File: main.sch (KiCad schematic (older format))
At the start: 25 parts, among them U3 PT6311, U4 VFD_HNV-12SS62

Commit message: shuffled things around
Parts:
- removed R40, R41, R42, R43, R44, R45, R46, R47: 10K, Resistor_SMD:R_0805_2012Metric, symbol Device:R
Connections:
- net labels removed: K1, K2, K3, K4
- wire segments 147 -> 120
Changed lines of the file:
@@
 	2400 3400 2400 3600
-Wire Wire Line
-	5700 5800 5800 5800
-$Comp
-L Device:R R41
-U 1 1 5F375184
-P 5800 6150
-F 0 "R41" H 5870 6196 50  0000 L CNN
-F 1 "10K" H 5870 6105 50  0000 L CNN
-F 2 "Resistor_SMD:R_0805_2012Metric" V 5730 6150 50  0001 C CNN
-F 3 "~" H 5800 6150 50  0001 C CNN
-	1    5800 6150
-	1    0    0    -1
-$EndComp
-$Comp
-L Device:R R43
-U 1 1 5F3751DC
-P 6100 6000
-F 0 "R43" H 6170 6046 50  0000 L CNN
-F 1 "10K" H 6170 5955 50  0000 L CNN
-F 2 "Resistor_SMD:R_0805_2012Metric" V 6030 6000 50  0001 C CNN
-F 3 "~" H 6100 6000 50  0001 C CNN
-	1    6100 6000
-	1    0    0    -1
-$EndComp
-$Comp
-L Device:R R45
-U 1 1 5F378B77
-P 6400 5850
-F 0 "R45" H 6470 5896 50  0000 L CNN
-F 1 "10K" H 6470 5805 50  0000 L CNN
-F 2 "Resistor_SMD:R_0805_2012Metric" V 6330 5850 50  0001 C CNN
-F 3 "~" H 6400 5850 50  0001 C CNN
-	1    6400 5850
-	1    0    0    -1
-$EndComp
-$Comp
-L Device:R R47
-U 1 1 5F37C669
-P 6700 5700
-F 0 "R47" H 6770 5746 50  0000 L CNN
-F 1 "10K" H 6770 5655 50  0000 L CNN
-F 2 "Resistor_SMD:R_0805_2012Metric" V 6630 5700 50  0001 C CNN
-F 3 "~" H 6700 5700 50  0001 C CNN
-	1    6700 5700
-	1    0    0    -1
-$EndComp
-Wire Wire Line
-	6700 5850 6700 6350
-Wire Wire Line
-	6700 6350 6400 6350
-Wire Wire Line
-	5800 6350 5800 6300
-Wire Wire Line
-	6100 6150 6100 6350
-Connection ~ 6100 6350
-Wire Wire Line
-	6100 6350 5800 6350
-Wire Wire Line
-	6400 6000 6400 6350
-Connection ~ 6400 6350
-Wire Wire Line
-	6400 6350 6250 6350
-Wire Wire Line
-	6250 6350 6250 6400
-Connection ~ 6250 6350
-Wire Wire Line
-	6250 6350 6100 6350
-$Comp
-L power:GND #PWR050
-U 1 1 5F38C73B
-P 6250 6400
-F 0 "#PWR050" H 6250 6150 50  0001 C CNN
-F 1 "GND" H 6255 6227 50  0000 C CNN
-F 2 "" H 6250 6400 50  0001 C CNN
-F 3 "" H 6250 6400 50  0001 C CNN
-	1    6250 6400
-	1    0    0    -1
-$EndComp
-Wire Wire Line
-	6700 5550 6700 5500
-Wire Wire Line
-	6400 5600 6400 5700
-Wire Wire Line
-	6100 5700 6100 5850
-Wire Wire Line
-	5800 5800 5800 6000
-Wire Wire Line
-	6700 5500 6750 5500
-Wire Wire Line
-	6400 5600 6450 5600
-Wire Wire Line
-	6100 5700 6150 5700
-Wire Wire Line
-	5800 5800 5850 5800
-Connection ~ 5800 5800
-Text HLabel 6750 5500 2    50   Input ~ 0
-K1
-Text HLabel 6450 5600 2    50   Input ~ 0
-K2
-Text HLabel 6150 5700 2    50   Input ~ 0
-K3
-Text HLabel 5850 5800 2    50   Input ~ 0
-K4
 Wire Wire Line
 	5350 2550 6500 2550
@@
 	4000 4500 3700 4500
 Wire Wire Line
-	3700 4700 3750 4700
-Wire Wire Line
 	3750 5100 4000 5100
 Wire Wire Line
-	3750 4700 3750 5100
-Wire Wire Line
 	3750 5100 3750 5200
-Connection ~ 3750 5100
 $Comp
 L power:GND #PWR047
@@
 	1800 2800 2250 2800
 $Comp
-L Device:R R44
-U 1 1 5F318CEB
-P 6150 5600
-F 0 "R44" V 5943 5600 50  0000 C CNN
-F 1 "10K" V 6034 5600 50  0000 C CNN
-F 2 "Resistor_SMD:R_0805_2012Metric" V 6080 5600 50  0001 C CNN
-F 3 "~" H 6150 5600 50  0001 C CNN
-	1    6150 5600
-	0    1    1    0
-$EndComp
-Wire Wire Line
-	6100 5700 6000 5700
-Connection ~ 6100 5700
-Wire Wire Line
-	6400 5600 6300 5600
-Connection ~ 6400 5600
-Wire Wire Line
-	6700 5500 6600 5500
-Connection ~ 6700 5500
-$Comp
-L Device:R R46
-U 1 1 5F33290D
-P 6450 5500
-F 0 "R46" V 6243 5500 50  0000 C CNN
-F 1 "10K" V 6334 5500 50  0000 C CNN
-F 2 "Resistor_SMD:R_0805_2012Metric" V 6380 5500 50  0001 C CNN
-F 3 "~" H 6450 5500 50  0001 C CNN
-	1    6450 5500
-	0    1    1    0
-$EndComp
-$Comp
-L Device:R R42
-U 1 1 5F343E3D
-P 5850 5700
-F 0 "R42" V 5643 5700 50  0000 C CNN
-F 1 "10K" V 5734 5700 50  0000 C CNN
-F 2 "Resistor_SMD:R_0805_2012Metric" V 5780 5700 50  0001 C CNN
-F 3 "~" H 5850 5700 50  0001 C CNN
-	1    5850 5700
-	0    1    1    0
-$EndComp
-$Comp
-L Device:R R40
-U 1 1 5F34C8CC
-P 5550 5800
-F 0 "R40" V 5343 5800 50  0000 C CNN
-F 1 "10K" V 5434 5800 50  0000 C CNN
-F 2 "Resistor_SMD:R_0805_2012Metric" V 5480 5800 50  0001 C CNN
-F 3 "~" H 5550 5800 50  0001 C CNN
-	1    5550 5800
-	0    1    1    0
-$EndComp
-Wire Wire Line
-	5350 5500 6300 5500
-Wire Wire Line
-	6000 5600 5350 5600
-Wire Wire Line
-	5350 5700 5700 5700
-Wire Wire Line
-	5400 5800 5350 5800
-$Comp
 L Connector:TestPoint TP1

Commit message: NTC circuit and values added
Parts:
- U3: symbol ThommasSTUFF:PT6311-Custom_modules -> buttonbox2-rescue:PT6311-Custom_modules-ThommasSTUFF
- U4: symbol ThommasSTUFF:VFD_HNV-12SS62-custom_comps -> buttonbox2-rescue:VFD_HNV-12SS62-custom_comps-ThommasSTUFF
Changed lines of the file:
@@
 $EndDescr
 $Comp
-L ThommasSTUFF:PT6311-Custom_modules U?
+L buttonbox2-rescue:PT6311-Custom_modules-ThommasSTUFF U?
 U 1 1 5F3F0EEF
 P 4650 2250
@@
 	5350 2350 5400 2350
 $Comp
-L ThommasSTUFF:VFD_HNV-12SS62-custom_comps U?
+L buttonbox2-rescue:VFD_HNV-12SS62-custom_comps-ThommasSTUFF U?
 U 1 1 5F3F0F03
 P 7500 1700

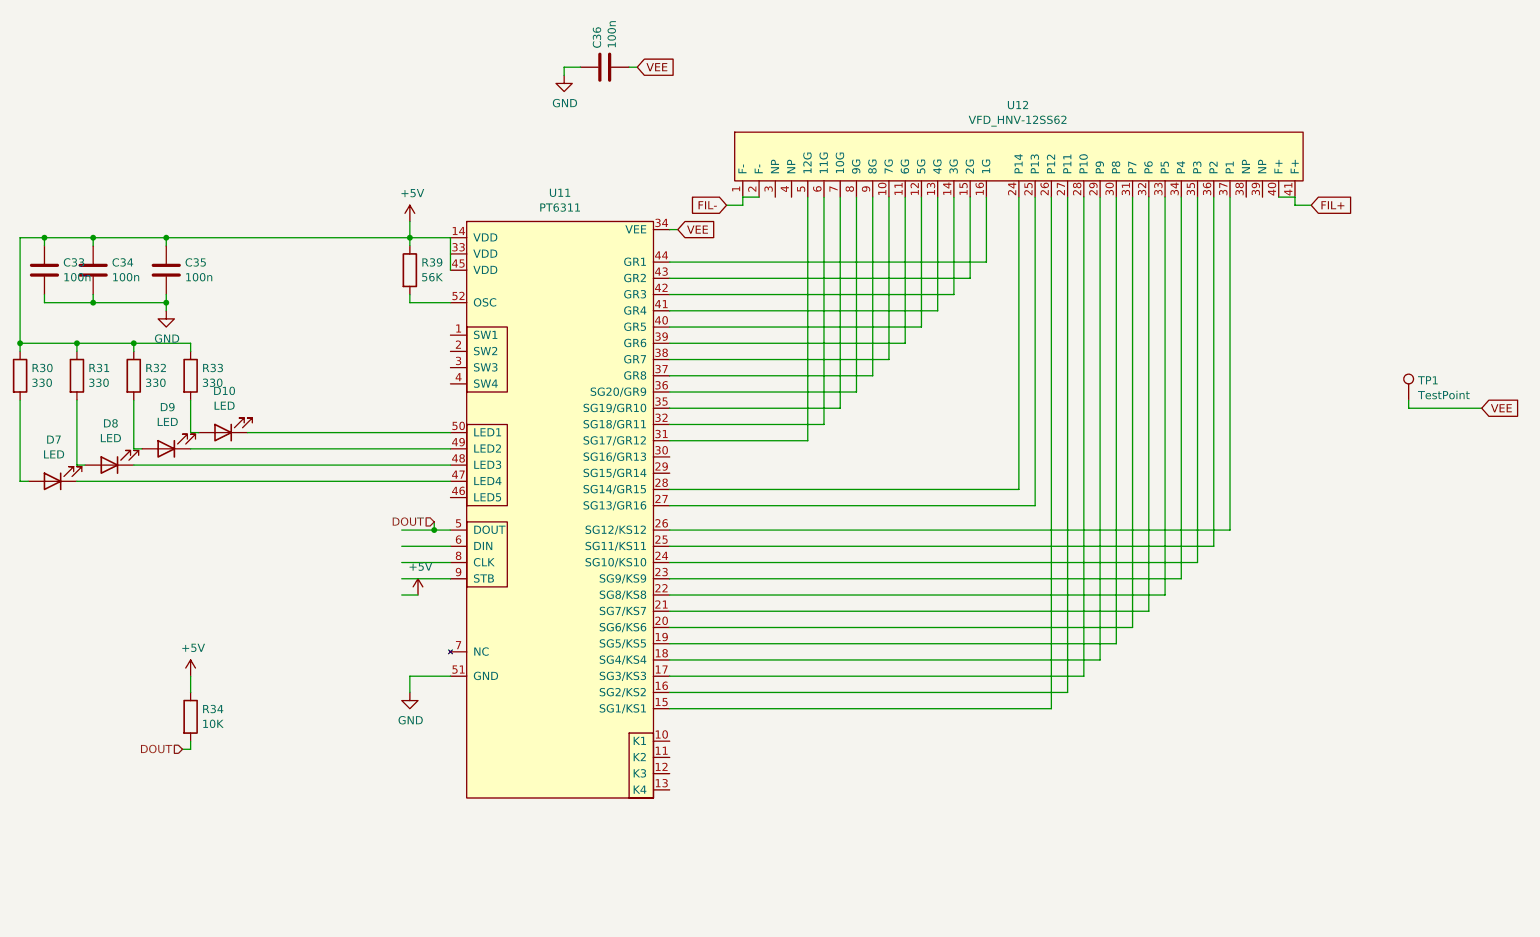
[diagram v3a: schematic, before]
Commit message: Fixed some DRC errors and some incorrect wiring
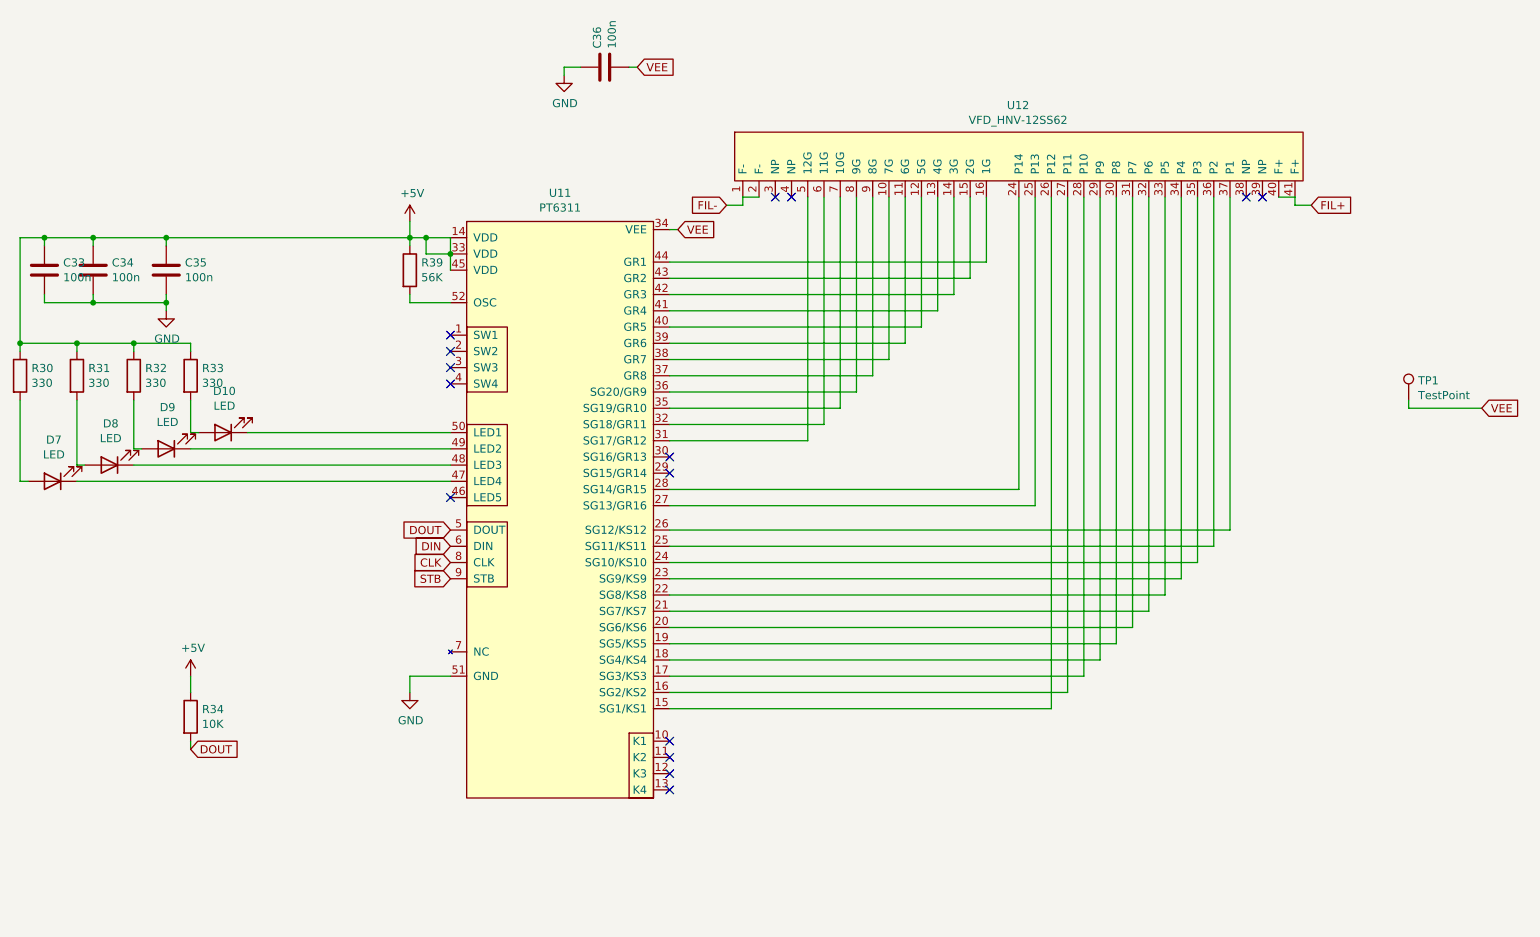
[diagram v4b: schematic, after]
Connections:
- net labels added: CLK, DIN, STB
- wire segments 120 -> 116
- no-connect marks 0 -> 15
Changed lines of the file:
@@
 $EndComp
 Wire Wire Line
-	3750 2400 4000 2400
+	3750 2400 3850 2400
 Wire Wire Line
 	3750 2800 4000 2800
@@
 	8800 4200 8800 2150
 Wire Wire Line
-	4000 4200 3900 4200
-Wire Wire Line
-	4000 4300 3700 4300
-Wire Wire Line
-	3700 4400 4000 4400
-Wire Wire Line
-	4000 4500 3700 4500
-Wire Wire Line
 	3750 5100 4000 5100
 Wire Wire Line
@@
 F 3 "" H 3750 5200 50  0001 C CNN
 	1    3750 5200
-	1    0    0    -1
-$EndComp
-Wire Wire Line
-	3700 4600 3800 4600
-$Comp
-L power:+5V #PWR048
-U 1 1 5F71F7BB
-P 3800 4600
-F 0 "#PWR048" H 3800 4450 50  0001 C CNN
-F 1 "+5V" H 3815 4773 50  0000 C CNN
-F 2 "" H 3800 4600 50  0001 C CNN
-F 3 "" H 3800 4600 50  0001 C CNN
-	1    3800 4600
 	1    0    0    -1
 $EndComp
@@
 	1    0    0    -1
 $EndComp
-Text HLabel 2350 5550 0    50   Input ~ 0
+Wire Wire Line
+	2400 5500 2400 5550
+Wire Wire Line
+	6400 3150 6700 3150
+Wire Wire Line
+	6500 2550 7300 2550
+Wire Wire Line
+	6600 2950 6900 2950
+Wire Wire Line
+	6800 2650 7200 2650
+Wire Wire Line
+	6900 2750 7100 2750
+Wire Wire Line
+	2750 3600 4000 3600
+Wire Wire Line
+	2400 3700 4000 3700
+Wire Wire Line
+	2050 3800 4000 3800
+Wire Wire Line
+	1700 3900 4000 3900
+Wire Wire Line
+	6500 2150 6500 3350
+Wire Wire Line
+	6800 2150 6800 3050
+Wire Wire Line
+	6900 2150 6900 2950
+Wire Wire Line
+	6600 2150 6600 3250
+Wire Wire Line
+	6400 2150 6400 3450
+Wire Wire Line
+	4000 2400 4000 2500
+Wire Wire Line
+	2250 2400 3750 2400
+NoConn ~ 9000 2150
+NoConn ~ 8900 2150
+NoConn ~ 6000 2150
+NoConn ~ 6100 2150
+NoConn ~ 5350 3750
+NoConn ~ 5350 3850
+NoConn ~ 5350 5500
+NoConn ~ 5350 5600
+NoConn ~ 5350 5700
+NoConn ~ 5350 5800
+NoConn ~ 4000 3000
+NoConn ~ 4000 3100
+NoConn ~ 4000 3200
+NoConn ~ 4000 3300
+NoConn ~ 4000 4000
+Text GLabel 4000 4200 0    50   Input ~ 0
 DOUT
-Text HLabel 3900 4150 0    50   Input ~ 0
+Text GLabel 4000 4300 0    50   Input ~ 0
+DIN
+Text GLabel 4000 4400 0    50   Input ~ 0
+CLK
+Text GLabel 4000 4500 0    50   Input ~ 0
+STB
+Wire Wire Line
+	4000 2500 3850 2500
+Wire Wire Line
+	3850 2500 3850 2400
+Connection ~ 4000 2500
+Wire Wire Line
+	4000 2500 4000 2600
+Connection ~ 3850 2400
+Wire Wire Line
+	3850 2400 4000 2400
+Text GLabel 2400 5550 2    50   Input ~ 0
 DOUT
-Wire Wire Line
-	3900 4150 3900 4200
-Connection ~ 3900 4200
-Wire Wire Line
-	3900 4200 3700 4200
-Wire Wire Line
-	2400 5500 2400 5550
-Wire Wire Line
-	2400 5550 2350 5550
-Wire Wire Line
-	6400 3150 6700 3150
-Wire Wire Line
-	6500 2550 7300 2550
-Wire Wire Line
-	6600 2950 6900 2950
-Wire Wire Line
-	6800 2650 7200 2650
-Wire Wire Line
-	6900 2750 7100 2750
-Wire Wire Line
-	2750 3600 4000 3600
-Wire Wire Line
-	2400 3700 4000 3700
-Wire Wire Line
-	2050 3800 4000 3800
-Wire Wire Line
-	1700 3900 4000 3900
-Wire Wire Line
-	6500 2150 6500 3350
-Wire Wire Line
-	6800 2150 6800 3050
-Wire Wire Line
-	6900 2150 6900 2950
-Wire Wire Line
-	6600 2150 6600 3250
-Wire Wire Line
-	6400 2150 6400 3450
-Wire Wire Line
-	4000 2400 4000 2600
-Wire Wire Line
-	2250 2400 3750 2400
 $EndSCHEMATC

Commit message: Changed a lot, ordered the final thing
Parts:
- added TP3, TP4: TestPoint, TestPoint:TestPoint_THTPad_D2.0mm_Drill1.0mm, symbol Connector:TestPoint
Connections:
- net FIL+: now also TP4.1
- net FIL-: now also TP3.1
- net +5V renamed +3V3
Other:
- moved on the sheet: R34
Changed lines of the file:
@@
 Wire Wire Line
 	3750 2300 3750 2400
-$Comp
-L power:+5V #PWR?
-U 1 1 5F3F0EFB
-P 3750 2300
-AR Path="/5F3F0EFB" Ref="#PWR?"  Part="1"
-AR Path="/5F3F0D8E/5F3F0EFB" Ref="#PWR07"  Part="1"
-AR Path="/60E90241/5F3F0EFB" Ref="#PWR046"  Part="1"
-F 0 "#PWR046" H 3750 2150 50  0001 C CNN
-F 1 "+5V" H 3765 2473 50  0000 C CNN
-F 2 "" H 3750 2300 50  0001 C CNN
-F 3 "" H 3750 2300 50  0001 C CNN
-	1    3750 2300
-	1    0    0    -1
-$EndComp
 Text GLabel 5400 2350 2    50   Input ~ 0
 VEE
@@
 	9200 2150 9200 2200
 Wire Wire Line
-	9200 2200 9300 2200
+	9200 2200 9250 2200
 Text GLabel 9300 2200 2    50   Input ~ 0
 FIL+
@@
 L Device:R R34
 U 1 1 5F4F75CE
-P 2400 5350
-F 0 "R34" H 2470 5396 50  0000 L CNN
-F 1 "10K" H 2470 5305 50  0000 L CNN
-F 2 "Resistor_SMD:R_0805_2012Metric" V 2330 5350 50  0001 C CNN
-F 3 "~" H 2400 5350 50  0001 C CNN
-	1    2400 5350
-	1    0    0    -1
-$EndComp
-Wire Wire Line
-	2400 5100 2400 5200
-$Comp
-L power:+5V #PWR?
-U 1 1 5F4F7CB7
-P 2400 5100
-AR Path="/5F4F7CB7" Ref="#PWR?"  Part="1"
-AR Path="/5F3F0D8E/5F4F7CB7" Ref="#PWR016"  Part="1"
-AR Path="/60E90241/5F4F7CB7" Ref="#PWR045"  Part="1"
-F 0 "#PWR045" H 2400 4950 50  0001 C CNN
-F 1 "+5V" H 2415 5273 50  0000 C CNN
-F 2 "" H 2400 5100 50  0001 C CNN
-F 3 "" H 2400 5100 50  0001 C CNN
-	1    2400 5100
-	1    0    0    -1
-$EndComp
-Wire Wire Line
-	2400 5500 2400 5550
+P 3150 4650
+F 0 "R34" H 3220 4696 50  0000 L CNN
+F 1 "10K" H 3220 4605 50  0000 L CNN
+F 2 "Resistor_SMD:R_0805_2012Metric" V 3080 4650 50  0001 C CNN
+F 3 "~" H 3150 4650 50  0001 C CNN
+	1    3150 4650
+	1    0    0    -1
+$EndComp
+Wire Wire Line
+	3150 4400 3150 4500
+Wire Wire Line
+	3150 4800 3150 4850
 Wire Wire Line
 	6400 3150 6700 3150
@@
 Wire Wire Line
 	3850 2400 4000 2400
-Text GLabel 2400 5550 2    50   Input ~ 0
+Text GLabel 3150 4850 2    50   Input ~ 0
 DOUT
+$Comp
+L Connector:TestPoint TP4
+U 1 1 60DFCA85
+P 9250 2200
+F 0 "TP4" H 9308 2320 50  0000 L CNN
+F 1 "TestPoint" H 9308 2229 50  0000 L CNN
+F 2 "TestPoint:TestPoint_THTPad_D2.0mm_Drill1.0mm" H 9450 2200 50  0001 C CNN
+F 3 "~" H 9450 2200 50  0001 C CNN
+	1    9250 2200
+	-1   0    0    1
+$EndComp
+Connection ~ 9250 2200
+Wire Wire Line
+	9250 2200 9300 2200
+$Comp
+L Connector:TestPoint TP3
+U 1 1 60DFD783
+P 5800 2200
+F 0 "TP3" H 5858 2320 50  0000 L CNN
+F 1 "TestPoint" H 5858 2229 50  0000 L CNN
+F 2 "TestPoint:TestPoint_THTPad_D2.0mm_Drill1.0mm" H 6000 2200 50  0001 C CNN
+F 3 "~" H 6000 2200 50  0001 C CNN
+	1    5800 2200
+	-1   0    0    1
+$EndComp
+Connection ~ 5800 2200
+$Comp
+L power:+3.3V #PWR045
+U 1 1 60E5680F
+P 3150 4400
+F 0 "#PWR045" H 3150 4250 50  0001 C CNN
+F 1 "+3.3V" H 3165 4573 50  0000 C CNN
+F 2 "" H 3150 4400 50  0001 C CNN
+F 3 "" H 3150 4400 50  0001 C CNN
+	1    3150 4400
+	1    0    0    -1
+$EndComp
+$Comp
+L power:+3.3V #PWR046
+U 1 1 60E5728D
+P 3750 2300
+F 0 "#PWR046" H 3750 2150 50  0001 C CNN
+F 1 "+3.3V" H 3765 2473 50  0000 C CNN
+F 2 "" H 3750 2300 50  0001 C CNN
+F 3 "" H 3750 2300 50  0001 C CNN
+	1    3750 2300
+	1    0    0    -1
+$EndComp
 $EndSCHEMATC
